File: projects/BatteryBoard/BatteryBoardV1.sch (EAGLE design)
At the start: 111 parts, among them M1 BSO201SP, U1 LTC4412MPS6, U2 SM74611, U3 LTC4121, U4 LTC4121, U5 LTC4121

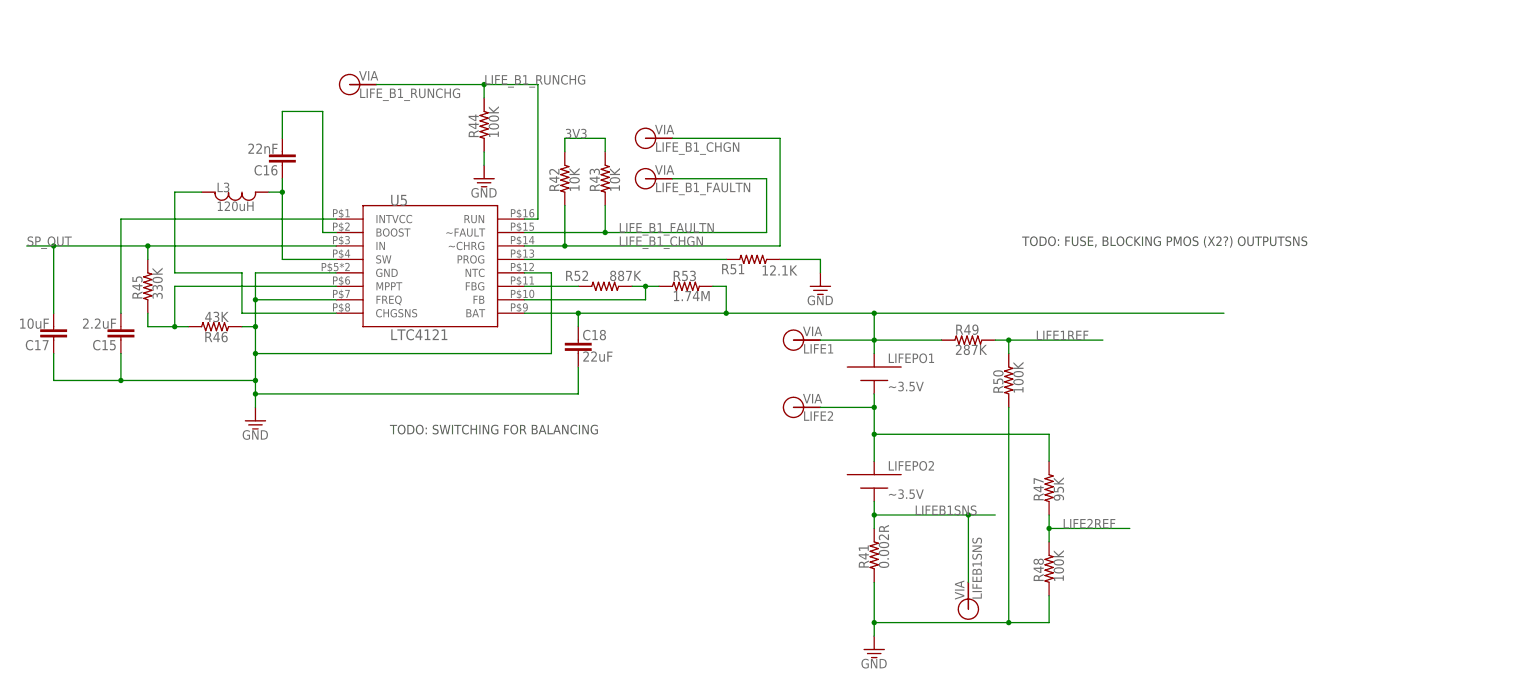
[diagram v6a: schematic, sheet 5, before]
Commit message: LiFePO4 Balancing added
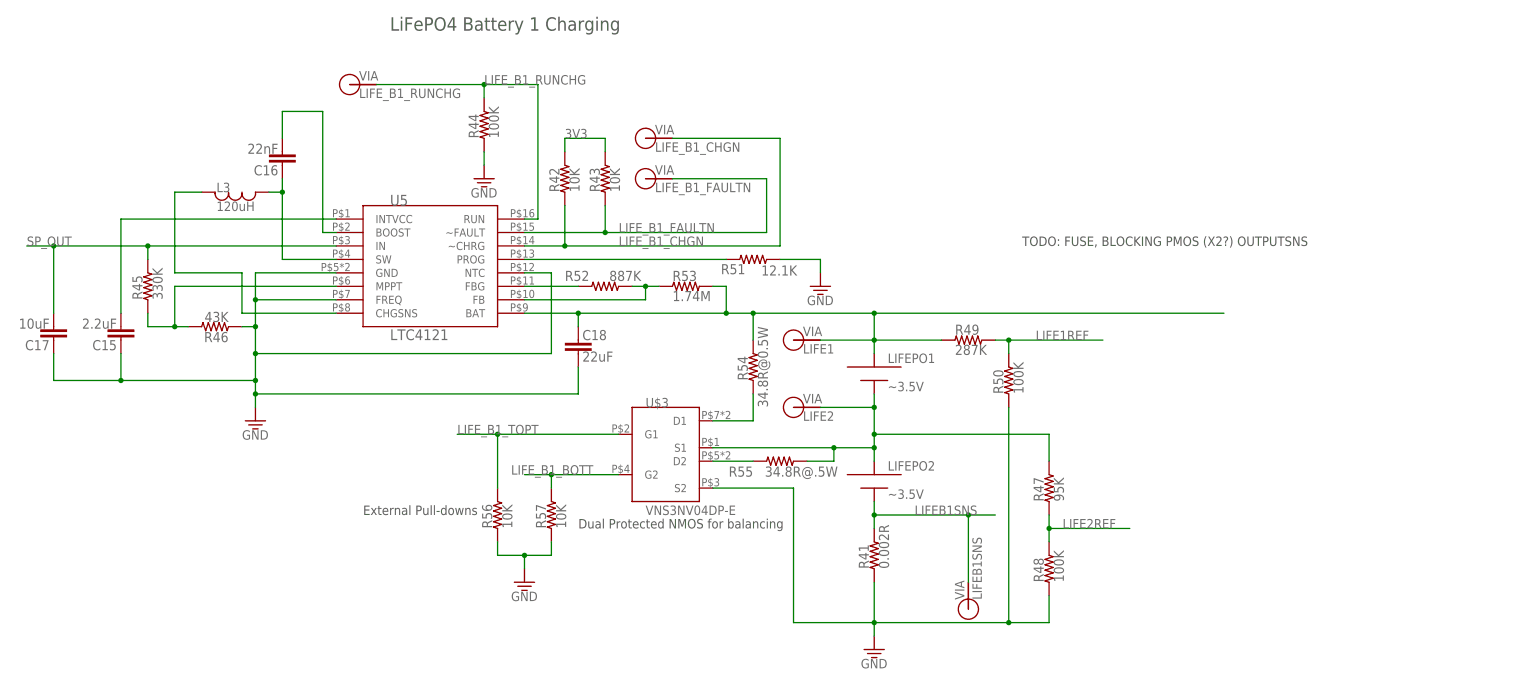
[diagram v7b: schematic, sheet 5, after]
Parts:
- added R54: 34.8R@0.5W, BrownSpaceEngineering:RES0805
- added R55: 34.8R@.5W, BrownSpaceEngineering:RES0805
- added R56, R57: 10K, BrownSpaceEngineering:RES0805
- added U$3: VNS3NV04DP-E, BrownSpaceEngineering:VNS3NV04DP-E
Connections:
- new net LIFE_B1_BOTT: R57.2, U$3.G2
- new net LIFE_B1_TOPT: R56.2, U$3.G1
- new net N$24: R54.1, U$3.D1
- new net N$25: R55.2, U$3.D2
- net GND: now also R56.1, R57.1, U$3.S2
- net LIFE1: now also R54.2
- net LIFE2: now also R55.1, U$3.S1
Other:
- note added: "Dual Protected NMOS for balancing"
- note added: "External Pull-downs"
- note added: "LiFePO4 Battery 1 Charging"
- note added: "Solar Panel Front End"
- note removed: "TODO: SWITCHING FOR BALANCING"
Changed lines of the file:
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@@
 <part name="V19" library="BrownSpaceEngineering" deviceset="VIA" device="" technology="60MIL" value="LIFE_B1_FAULTN"/>
 <part name="C18" library="BrownSpaceEngineering" deviceset="CAP" device="0805" value="22uF"/>
+<part name="U$3" library="BrownSpaceEngineering" deviceset="VNS3NV04DP-E" device=""/>
+<part name="R54" library="BrownSpaceEngineering" deviceset="RES" device="0805" value="34.8R@0.5W"/>
+<part name="R55" library="BrownSpaceEngineering" deviceset="RES" device="0805" value="34.8R@.5W"/>
+<part name="R56" library="BrownSpaceEngineering" deviceset="RES" device="0805" value="10K"/>
+<part name="R57" library="BrownSpaceEngineering" deviceset="RES" device="0805" value="10K"/>
+<part name="GND23" library="supply1" deviceset="GND" device=""/>
 </parts>
 <sheets>
@@
 <wire x1="157.48" y1="66.04" x2="139.7" y2="66.04" width="0.254" layer="97" style="shortdash"/>
 <text x="142.24" y="93.98" size="1.778" layer="97">Current Sense Option</text>
+<text x="66.04" y="134.62" size="2.54" layer="97">Solar Panel Front End</text>
 </plain>
 <instances>
@@
 <plain>
 <text x="180.34" y="53.34" size="1.778" layer="97">TODO: FUSE, BLOCKING PMOS (X2?) OUTPUTSNS</text>
-<text x="60.96" y="17.78" size="1.778" layer="97">TODO: SWITCHING FOR BALANCING</text>
+<text x="60.96" y="93.98" size="2.54" layer="97">LiFePO4 Battery 1 Charging</text>
+<text x="55.88" y="2.54" size="1.778" layer="97">External Pull-downs</text>
+<text x="96.52" y="0" size="1.778" layer="97">Dual Protected NMOS for balancing</text>
 </plain>
 <instances>
@@
 <instance part="V19" gate="G$1" x="109.22" y="66.04"/>
 <instance part="C18" gate="G$1" x="96.52" y="33.02"/>
+<instance part="U$3" gate="G$1" x="111.76" y="12.7"/>
+<instance part="R54" gate="R$1" x="129.54" y="30.48" smashed="yes" rot="R90">
+<attribute name="NAME" x="128.524" y="27.94" size="1.905" layer="95" rot="R90"/>
+<attribute name="VALUE" x="132.334" y="22.86" size="1.905" layer="96" rot="R90"/>
+</instance>
+<instance part="R55" gate="R$1" x="134.62" y="12.7" smashed="yes" rot="R180">
+<attribute name="NAME" x="129.54" y="11.684" size="1.905" layer="95" rot="R180"/>
+<attribute name="VALUE" x="145.542" y="11.684" size="1.905" layer="96" rot="R180"/>
+</instance>
+<instance part="R56" gate="R$1" x="81.28" y="2.54" rot="R90"/>
+<instance part="R57" gate="R$1" x="91.44" y="2.54" rot="R90"/>
+<instance part="GND23" gate="1" x="86.36" y="-10.16"/>
 </instances>
 <busses>
@@
 <wire x1="177.8" y1="-17.78" x2="177.8" y2="22.86" width="0.1524" layer="91"/>
 <junction x="177.8" y="-17.78"/>
+<pinref part="U$3" gate="G$1" pin="S2"/>
+<wire x1="121.92" y1="7.62" x2="137.16" y2="7.62" width="0.1524" layer="91"/>
+<wire x1="137.16" y1="7.62" x2="137.16" y2="-17.78" width="0.1524" layer="91"/>
+<wire x1="137.16" y1="-17.78" x2="152.4" y2="-17.78" width="0.1524" layer="91"/>
 </segment>
 <segment>
@@
 <wire x1="134.62" y1="50.8" x2="142.24" y2="50.8" width="0.1524" layer="91"/>
 <wire x1="142.24" y1="50.8" x2="142.24" y2="48.26" width="0.1524" layer="91"/>
+</segment>
+<segment>
+<pinref part="R57" gate="R$1" pin="1"/>
+<wire x1="91.44" y1="-2.54" x2="91.44" y2="-5.08" width="0.1524" layer="91"/>
+<pinref part="GND23" gate="1" pin="GND"/>
+<wire x1="91.44" y1="-5.08" x2="86.36" y2="-5.08" width="0.1524" layer="91"/>
+<wire x1="86.36" y1="-5.08" x2="86.36" y2="-7.62" width="0.1524" layer="91"/>
+<pinref part="R56" gate="R$1" pin="1"/>
+<wire x1="81.28" y1="-2.54" x2="81.28" y2="-5.08" width="0.1524" layer="91"/>
+<wire x1="81.28" y1="-5.08" x2="86.36" y2="-5.08" width="0.1524" layer="91"/>
+<junction x="86.36" y="-5.08"/>
 </segment>
 </net>
@@
 <pinref part="LIFEPO2" gate="G$1" pin="PLUS"/>
 <pinref part="LIFEPO1" gate="G$1" pin="MINUS"/>
-<wire x1="152.4" y1="12.7" x2="152.4" y2="17.78" width="0.1524" layer="91"/>
+<wire x1="152.4" y1="12.7" x2="152.4" y2="15.24" width="0.1524" layer="91"/>
+<wire x1="152.4" y1="15.24" x2="152.4" y2="17.78" width="0.1524" layer="91"/>
 <wire x1="152.4" y1="17.78" x2="152.4" y2="22.86" width="0.1524" layer="91"/>
 <wire x1="152.4" y1="22.86" x2="152.4" y2="25.4" width="0.1524" layer="91"/>
@@
 <wire x1="142.24" y1="22.86" x2="152.4" y2="22.86" width="0.1524" layer="91"/>
 <junction x="152.4" y="22.86"/>
+<pinref part="U$3" gate="G$1" pin="S1"/>
+<wire x1="121.92" y1="15.24" x2="144.78" y2="15.24" width="0.1524" layer="91"/>
+<junction x="152.4" y="15.24"/>
+<pinref part="R55" gate="R$1" pin="1"/>
+<wire x1="144.78" y1="15.24" x2="152.4" y2="15.24" width="0.1524" layer="91"/>
+<wire x1="139.7" y1="12.7" x2="144.78" y2="12.7" width="0.1524" layer="91"/>
+<wire x1="144.78" y1="12.7" x2="144.78" y2="15.24" width="0.1524" layer="91"/>
+<junction x="144.78" y="15.24"/>
 </segment>
 </net>
@@
 <wire x1="152.4" y1="33.02" x2="152.4" y2="35.56" width="0.1524" layer="91"/>
 <wire x1="152.4" y1="35.56" x2="152.4" y2="40.64" width="0.1524" layer="91"/>
-<wire x1="152.4" y1="40.64" x2="124.46" y2="40.64" width="0.1524" layer="91"/>
+<wire x1="152.4" y1="40.64" x2="129.54" y2="40.64" width="0.1524" layer="91"/>
 <pinref part="R49" gate="R$1" pin="1"/>
+<wire x1="129.54" y1="40.64" x2="124.46" y2="40.64" width="0.1524" layer="91"/>
 <wire x1="124.46" y1="40.64" x2="96.52" y2="40.64" width="0.1524" layer="91"/>
 <wire x1="96.52" y1="40.64" x2="86.36" y2="40.64" width="0.1524" layer="91"/>
@@
 <wire x1="96.52" y1="40.64" x2="96.52" y2="38.1" width="0.1524" layer="91"/>
 <junction x="96.52" y="40.64"/>
+<pinref part="R54" gate="R$1" pin="2"/>
+<wire x1="129.54" y1="40.64" x2="129.54" y2="35.56" width="0.1524" layer="91"/>
+<junction x="129.54" y="40.64"/>
 </segment>
 </net>
@@
 </segment>
 </net>
+<net name="N$24" class="0">
+<segment>
+<pinref part="U$3" gate="G$1" pin="D1"/>
+<pinref part="R54" gate="R$1" pin="1"/>
+<wire x1="121.92" y1="20.32" x2="129.54" y2="20.32" width="0.1524" layer="91"/>
+<wire x1="129.54" y1="20.32" x2="129.54" y2="25.4" width="0.1524" layer="91"/>
+</segment>
+</net>
+<net name="N$25" class="0">
+<segment>
+<pinref part="R55" gate="R$1" pin="2"/>
+<pinref part="U$3" gate="G$1" pin="D2"/>
+<wire x1="129.54" y1="12.7" x2="121.92" y2="12.7" width="0.1524" layer="91"/>
+</segment>
+</net>
+<net name="LIFE_B1_BOTT" class="0">
+<segment>
+<pinref part="U$3" gate="G$1" pin="G2"/>
+<pinref part="R57" gate="R$1" pin="2"/>
+<wire x1="104.14" y1="10.16" x2="91.44" y2="10.16" width="0.1524" layer="91"/>
+<wire x1="91.44" y1="10.16" x2="91.44" y2="7.62" width="0.1524" layer="91"/>
+<wire x1="91.44" y1="10.16" x2="86.36" y2="10.16" width="0.1524" layer="91"/>
+<junction x="91.44" y="10.16"/>
+<label x="83.82" y="10.16" size="1.778" layer="95"/>
+</segment>
+</net>
+<net name="LIFE_B1_TOPT" class="0">
+<segment>
+<pinref part="U$3" gate="G$1" pin="G1"/>
+<wire x1="104.14" y1="17.78" x2="81.28" y2="17.78" width="0.1524" layer="91"/>
+<pinref part="R56" gate="R$1" pin="2"/>
+<wire x1="81.28" y1="17.78" x2="81.28" y2="7.62" width="0.1524" layer="91"/>
+<wire x1="81.28" y1="17.78" x2="73.66" y2="17.78" width="0.1524" layer="91"/>
+<junction x="81.28" y="17.78"/>
+<label x="73.66" y="17.78" size="1.778" layer="95"/>
+</segment>
+</net>

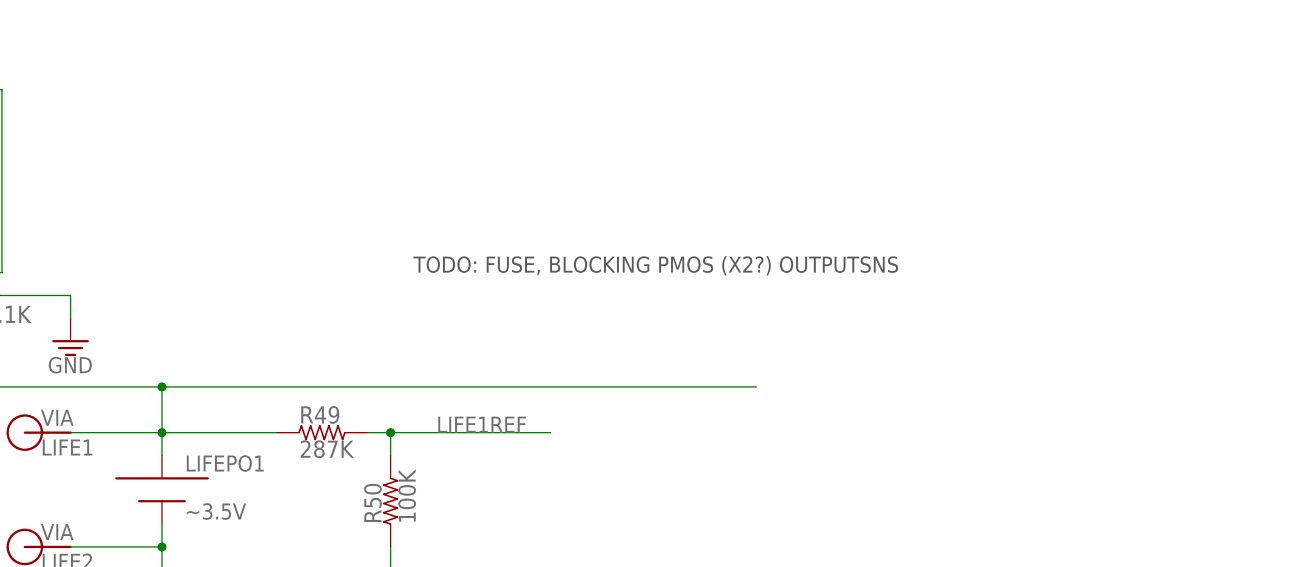
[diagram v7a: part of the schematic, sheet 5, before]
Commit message: Small Updates to Battery Board and BSE library
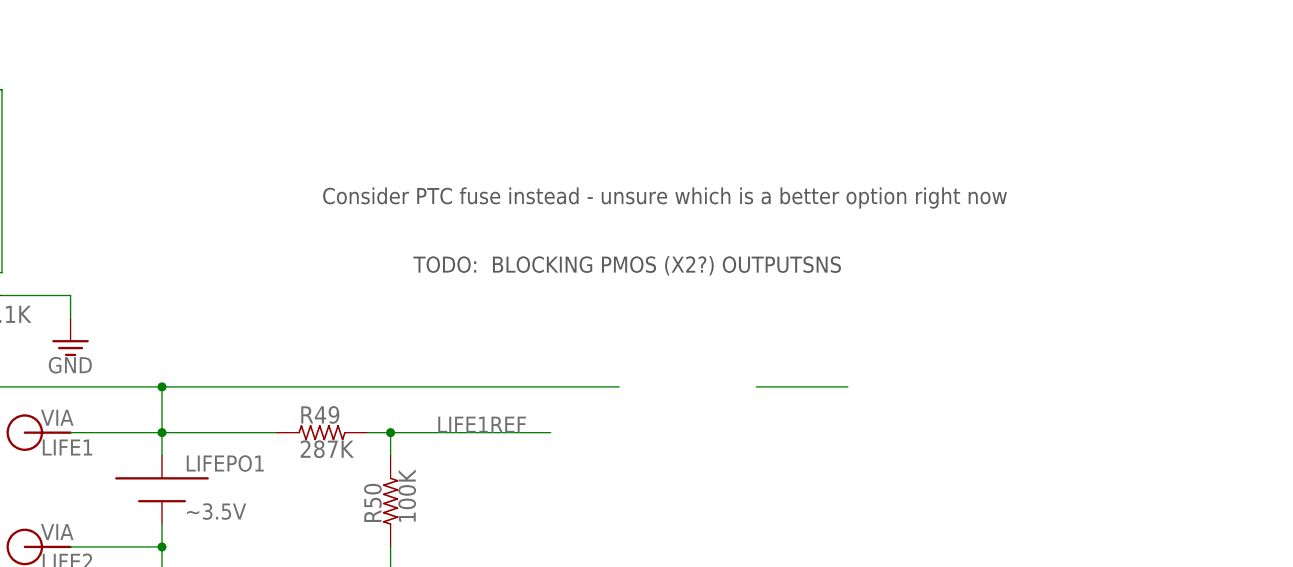
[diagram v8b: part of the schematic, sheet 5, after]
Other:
- note added: "Consider PTC fuse instead - unsure which is a better option right now"
- note added: "TODO: BLOCKING PMOS (X2?) OUTPUTSNS"
- note removed: "TODO: FUSE, BLOCKING PMOS (X2?) OUTPUTSNS"
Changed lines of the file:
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@@
 <description>LiFePO4 Battery 1 Charging</description>
 <plain>
-<text x="180.34" y="53.34" size="1.778" layer="97">TODO: FUSE, BLOCKING PMOS (X2?) OUTPUTSNS</text>
+<text x="180.34" y="53.34" size="1.778" layer="97">TODO:  BLOCKING PMOS (X2?) OUTPUTSNS</text>
 <text x="60.96" y="93.98" size="2.54" layer="97">LiFePO4 Battery 1 Charging</text>
 <text x="55.88" y="2.54" size="1.778" layer="97">External Pull-downs</text>
 <text x="96.52" y="0" size="1.778" layer="97">Dual Protected NMOS for balancing</text>
+<text x="170.18" y="60.96" size="1.778" layer="97">Consider PTC fuse instead - unsure which is a better option right now</text>
 </plain>
 <instances>
@@
 <pinref part="V17" gate="G$1" pin="P$1"/>
 <wire x1="142.24" y1="35.56" x2="152.4" y2="35.56" width="0.1524" layer="91"/>
-<wire x1="152.4" y1="40.64" x2="218.44" y2="40.64" width="0.1524" layer="91"/>
+<wire x1="152.4" y1="40.64" x2="203.2" y2="40.64" width="0.1524" layer="91"/>
 <junction x="152.4" y="40.64"/>
 <pinref part="C18" gate="G$1" pin="P$1"/>
@@
 </segment>
 </net>
+<net name="N$33" class="0">
+<segment>
+<wire x1="218.44" y1="40.64" x2="228.6" y2="40.64" width="0.1524" layer="91"/>
+</segment>
+</net>
